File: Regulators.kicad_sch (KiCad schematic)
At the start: 26 parts, among them J5 24V Logic, J6 24V Peripheral, U2 TPS5430DDAR, U3 TPS5430DDAR

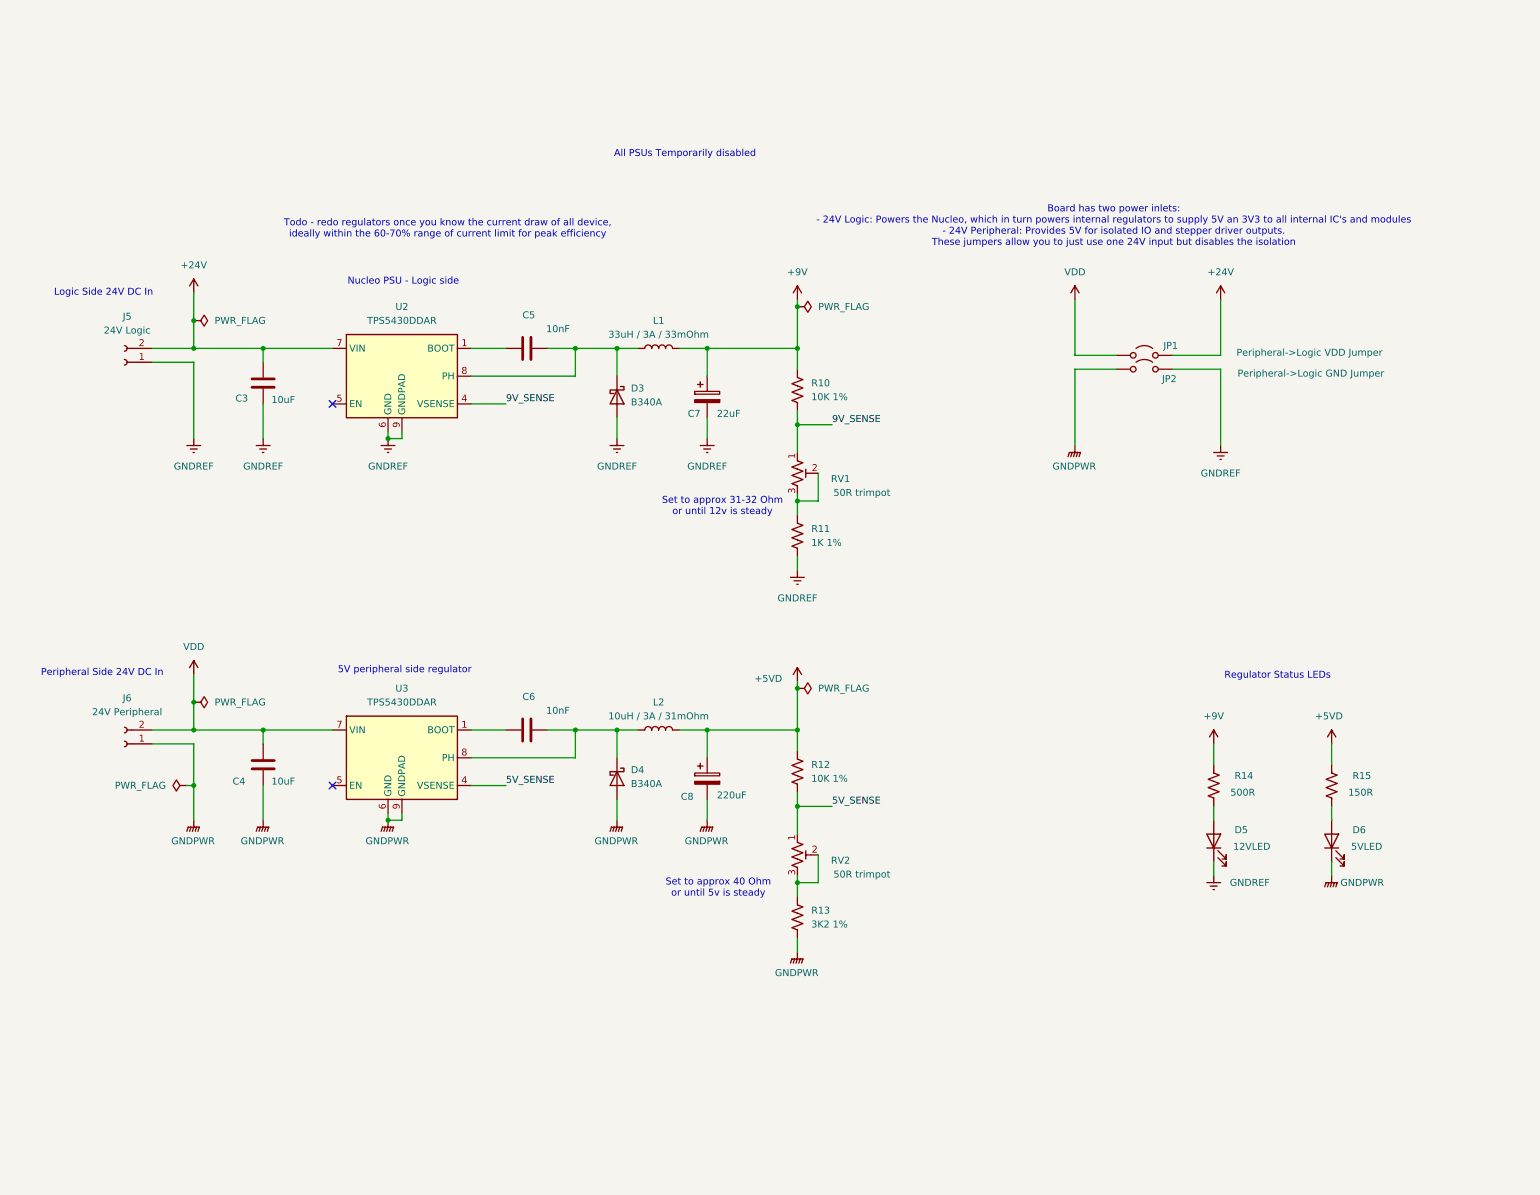
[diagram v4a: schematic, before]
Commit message: BOM consolidation for various resistors. Moved BOM into symbol libraries and updated supplimentary BOM. Switched IO optical isolation circuitry to a more cost effective part.
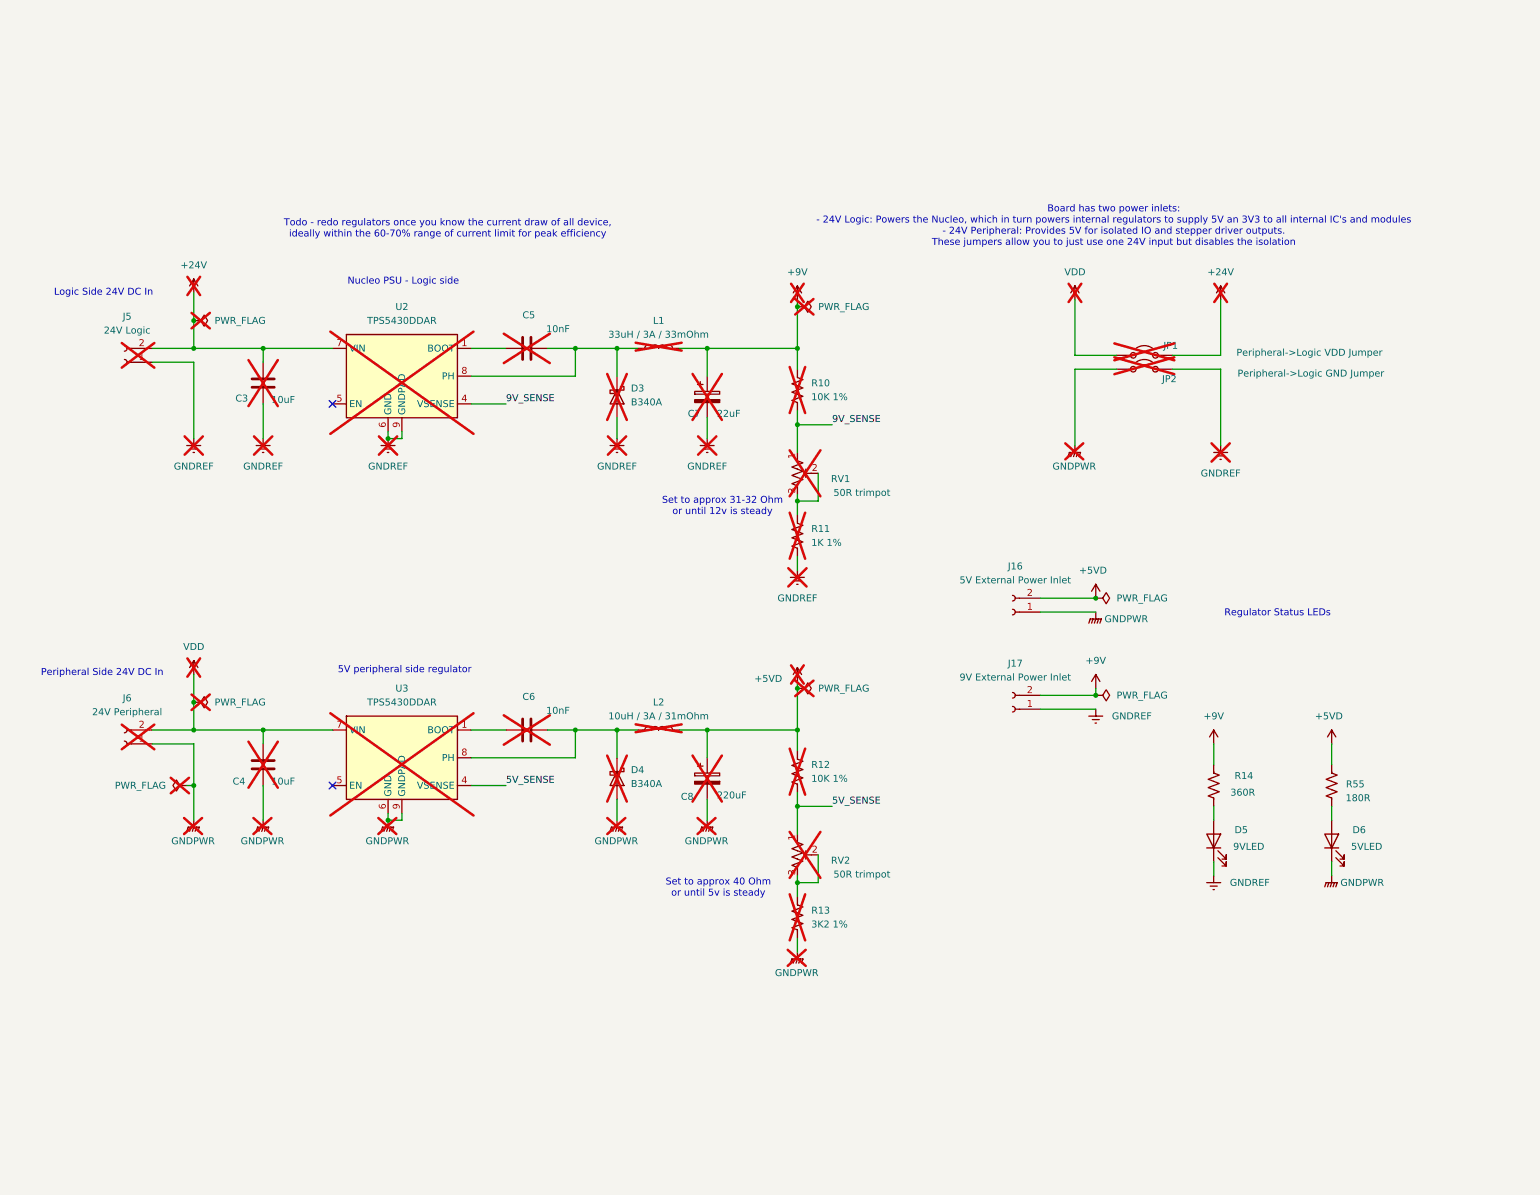
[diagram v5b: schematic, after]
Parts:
- removed R15: 150R, Resistor_SMD:R_1206_3216Metric_Pad1.30x1.75mm_HandSolder, symbol Device:R_US
- added J16: 5V External Power Inlet, EBWA_02_A:ADAMTECH_EBWA-02-A, symbol Connector:Conn_01x02_Socket
- added J17: 9V External Power Inlet, EBWA_02_A:ADAMTECH_EBWA-02-A, symbol Connector:Conn_01x02_Socket
- added R55: 180R, Resistor_SMD:R_1206_3216Metric_Pad1.30x1.75mm_HandSolder, symbol Device:R_US
- C3, C4, C5, C6, C7, C8, D3, D4, J5, J6, L1, L2, R10, R11, R12, R13: now not fitted
- D5: value 12VLED -> 9VLED
- JP1, JP2: Digikey Part Number (none) -> N/A; Digikey URL (none) -> N/A; now not fitted
- R14: value 500R -> 360R; Digikey Part Number (none) -> RMCF1206JT360RCT-ND; Digikey URL (none) -> https://www.digikey.com.au/en/products/detail/stackpole-ele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
- RV1, RV2: JLCPCB Part #（optional） C56340 -> (none); now not fitted
- U2, U3: JLCPCB Part #（optional） C9864 -> (none); now not fitted
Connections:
- net +5VD: now also J16.2 (Pin_2), R55.1
- net +9V: now also J17.2 (Pin_2)
- net GNDPWR: now also J16.1 (Pin_1)
- net GNDREF: now also J17.1 (Pin_1)
- net at D6.2 (A): now also R55.2
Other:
- note removed: "All PSUs Temporarily disabled"

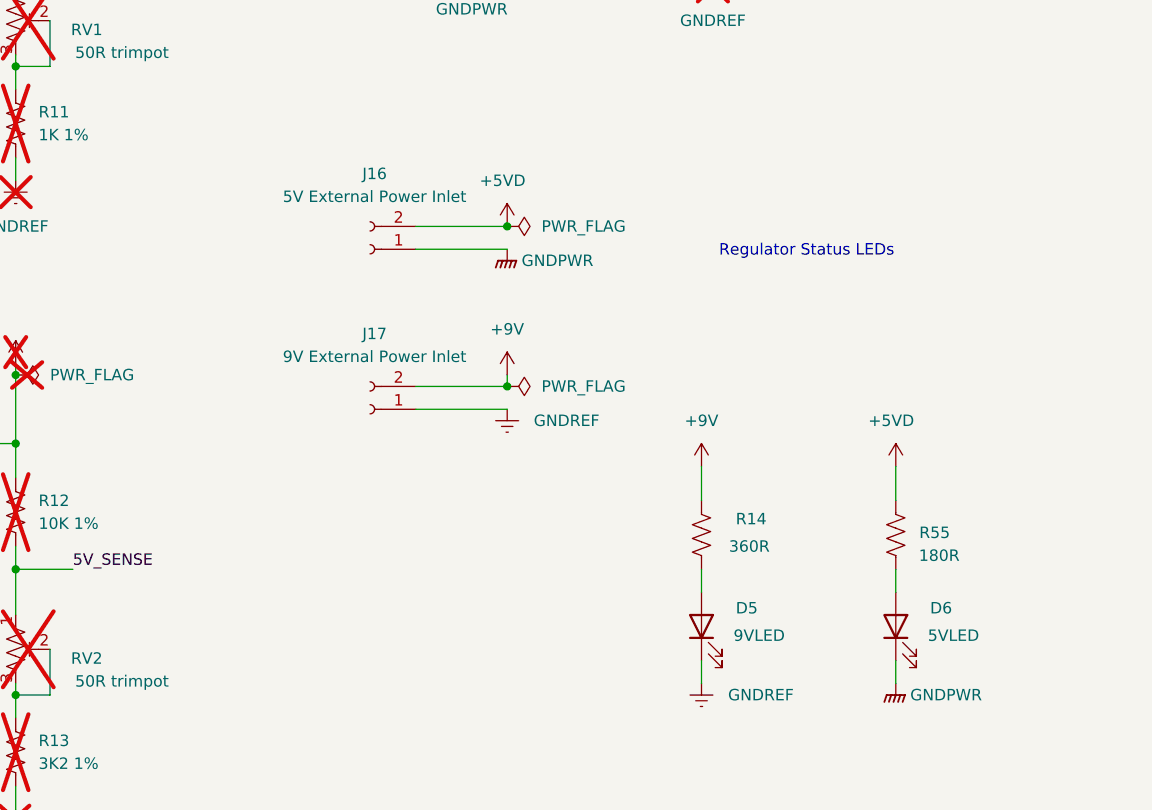
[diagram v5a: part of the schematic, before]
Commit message: more BOM consolidation. Switched out IO for vertical toolless wire to board terminals and added footprints. Put new isolated ground plane on board.
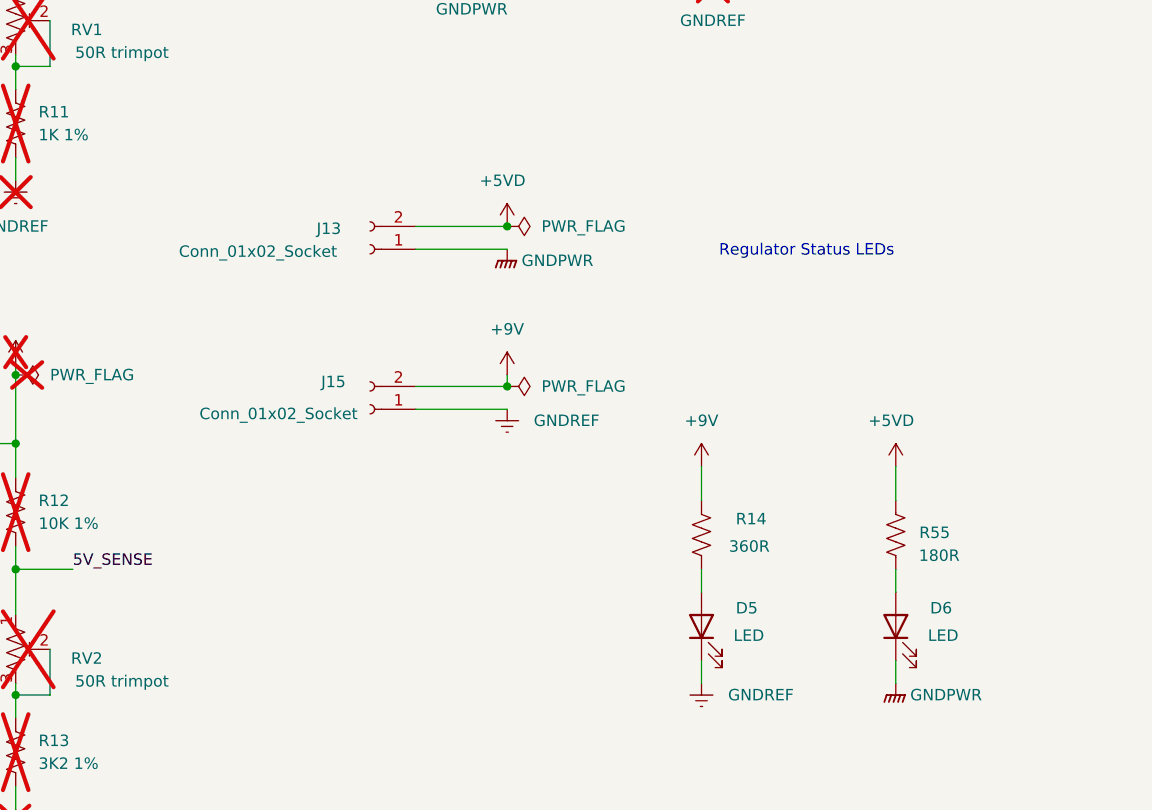
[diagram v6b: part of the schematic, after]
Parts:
- removed J16: 5V External Power Inlet, EBWA_02_A:ADAMTECH_EBWA-02-A, symbol Connector:Conn_01x02_Socket
- removed J17: 9V External Power Inlet, EBWA_02_A:ADAMTECH_EBWA-02-A, symbol Connector:Conn_01x02_Socket
- added J13, J15: Conn_01x02_Socket, Amphenol QT:QT02ADP83V0000G, symbol Connector:Conn_01x02_Socket
- D5: value 9VLED -> LED
- D6: value 5VLED -> LED
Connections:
- net +5VD: now also J13.2 (Pin_2)
- net +9V: now also J15.2 (Pin_2)
- net GNDPWR: now also J13.1 (Pin_1)
- net GNDREF: now also J15.1 (Pin_1)
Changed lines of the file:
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@@
-	)
-	(symbol
-		(lib_id "Connector:Conn_01x02_Socket")
-		(at 201.93 99.06 180)
-		(unit 1)
-		(exclude_from_sim no)
-		(in_bom yes)
-		(on_board yes)
-		(dnp no)
-		(property "Reference" "J16"
-			(at 202.438 90.678 0)
-			(effects
-				(font
-					(size 1.27 1.27)
-				)
-			)
-		)
-		(property "Value" "5V External Power Inlet"
-			(at 202.438 93.218 0)
-			(effects
-				(font
-					(size 1.27 1.27)
-				)
-			)
-		)
-		(property "Footprint" "EBWA_02_A:ADAMTECH_EBWA-02-A"
-			(at 201.93 99.06 0)
-			(effects
-				(font
-					(size 1.27 1.27)
-				)
-				(hide yes)
-			)
-		)
-		(property "Datasheet" "~"
-			(at 201.93 99.06 0)
-			(effects
-				(font
-					(size 1.27 1.27)
-				)
-				(hide yes)
-			)
-		)
-		(property "Description" "Generic connector, single row, 01x02, script generated"
-			(at 201.93 99.06 0)
-			(effects
-				(font
-					(size 1.27 1.27)
-				)
-				(hide yes)
-			)
-		)
-		(property "Digikey Part Number" "2057-EBWA-02-A-ND"
-			(at 201.93 99.06 0)
-			(effects
-				(font
-					(size 1.27 1.27)
-				)
-				(hide yes)
-			)
-		)
-		(property "Digikey URL" "https://www.digikey.com.au/en/products/detail/adam-tech/EBWA-02-A/9830631"
-			(at 201.93 99.06 0)
-			(effects
-				(font
-					(size 1.27 1.27)
-				)
-				(hide yes)
-			)
-		)
-		(pin "1"
-		)
-		(pin "2"
-		)
-		(instances
-			(project "Remora Nucleo F446ZE Hat"
-				(path "/5473abc6-7b93-43cc-a401-f691c4d7d7cf/e0dc83df-f7d9-4488-bd0b-6c0af36f8703"
-					(reference "J16")
-					(unit 1)
-				)
-			)
-		)
 	)
 	(symbol
@@
 			)
 		)
-		(property "Value" "5VLED"
+		(property "Value" "LED"
 			(at 263.906 141.986 90)
 			(effects
@@
 			)
 		)
-		(property "Value" "9VLED"
+		(property "Value" "LED"
 			(at 242.316 141.986 90)
 			(effects
@@
 	)
 	(symbol
-		(lib_id "Connector:Conn_01x02_Socket")
-		(at 201.93 116.84 180)
-		(unit 1)
-		(exclude_from_sim no)
-		(in_bom yes)
-		(on_board yes)
-		(dnp no)
-		(property "Reference" "J17"
-			(at 202.438 108.458 0)
-			(effects
-				(font
-					(size 1.27 1.27)
-				)
-			)
-		)
-		(property "Value" "9V External Power Inlet"
-			(at 202.438 110.998 0)
-			(effects
-				(font
-					(size 1.27 1.27)
-				)
-			)
-		)
-		(property "Footprint" "EBWA_02_A:ADAMTECH_EBWA-02-A"
-			(at 201.93 116.84 0)
-			(effects
-				(font
-					(size 1.27 1.27)
-				)
-				(hide yes)
-			)
-		)
-		(property "Datasheet" "~"
-			(at 201.93 116.84 0)
-			(effects
-				(font
-					(size 1.27 1.27)
-				)
-				(hide yes)
-			)
-		)
-		(property "Description" "Generic connector, single row, 01x02, script generated"
-			(at 201.93 116.84 0)
-			(effects
-				(font
-					(size 1.27 1.27)
-				)
-				(hide yes)
-			)
-		)
-		(property "Digikey Part Number" "2057-EBWA-02-A-ND"
-			(at 201.93 116.84 0)
-			(effects
-				(font
-					(size 1.27 1.27)
-				)
-				(hide yes)
-			)
-		)
-		(property "Digikey URL" "https://www.digikey.com.au/en/products/detail/adam-tech/EBWA-02-A/9830631"
-			(at 201.93 116.84 0)
-			(effects
-				(font
-					(size 1.27 1.27)
-				)
-				(hide yes)
-			)
-		)
-		(pin "1"
-		)
-		(pin "2"
-		)
-		(instances
-			(project "Remora Nucleo F446ZE Hat"
-				(path "/5473abc6-7b93-43cc-a401-f691c4d7d7cf/e0dc83df-f7d9-4488-bd0b-6c0af36f8703"
-					(reference "J17")
-					(unit 1)
-				)
-			)
-		)
-	)
-	(symbol
 		(lib_id "power:PWR_FLAG")
 		(at 52.07 115.57 270)
@@
 	)
 	(symbol
+		(lib_id "Connector:Conn_01x02_Socket")
+		(at 201.93 116.84 180)
+		(unit 1)
+		(exclude_from_sim no)
+		(in_bom yes)
+		(on_board yes)
+		(dnp no)
+		(property "Reference" "J15"
+			(at 197.866 113.792 0)
+			(effects
+				(font
+					(size 1.27 1.27)
+				)
+			)
+		)
+		(property "Value" "Conn_01x02_Socket"
+			(at 191.77 117.348 0)
+			(effects
+				(font
+					(size 1.27 1.27)
+				)
+			)
+		)
+		(property "Footprint" "Amphenol QT:QT02ADP83V0000G"
+			(at 201.93 116.84 0)
+			(effects
+				(font
+					(size 1.27 1.27)
+				)
+				(hide yes)
+			)
+		)
+		(property "Datasheet" "~"
+			(at 201.93 116.84 0)
+			(effects
+				(font
+					(size 1.27 1.27)
+				)
+				(hide yes)
+			)
+		)
+		(property "Description" "Generic connector, single row, 01x02, script generated"
+			(at 201.93 116.84 0)
+			(effects
+				(font
+					(size 1.27 1.27)
+				)
+				(hide yes)
+			)
+		)
+		(property "Digikey Part Number" "1818-QT04ADP83V0000G-ND"
+			(at 202.565 109.22 0)
+			(effects
+				(font
+					(size 1.27 1.27)
+				)
+				(hide yes)
+			)
+		)
+		(property "Digikey URL" "https://www.digikey.com.au/en/products/detail/amphenol-anytek/QT04ADP83V0000G/25618782"
+			(at 202.565 111.76 0)
+			(effects
+				(font
+					(size 1.27 1.27)
+				)
+				(hide yes)
+			)
+		)
+		(pin "1"
+		)
+		(pin "2"
+		)
+		(instances
+			(project "Remora Nucleo F446ZE Hat"
+				(path "/5473abc6-7b93-43cc-a401-f691c4d7d7cf/e0dc83df-f7d9-4488-bd0b-6c0af36f8703"
+					(reference "J15")
+					(unit 1)
+				)
+			)
+		)
+	)
+	(symbol
 		(lib_id "Device:R_US")
 		(at 162.56 154.94 0)
@@
 					(unit 1)
 				)
+			)
+		)
+	)
+	(symbol
+		(lib_id "Connector:Conn_01x02_Socket")
+		(at 201.93 99.06 180)
+		(unit 1)
+		(exclude_from_sim no)
+		(in_bom yes)
+		(on_board yes)
+		(dnp no)
+		(property "Reference" "J13"
+			(at 197.358 96.774 0)
+			(effects
+				(font
+					(size 1.27 1.27)
+				)
+			)
+		)
+		(property "Value" "Conn_01x02_Socket"
+			(at 189.484 99.314 0)
+			(effects
+				(font
+					(size 1.27 1.27)
+				)
+			)
+		)
+		(property "Footprint" "Amphenol QT:QT02ADP83V0000G"
+			(at 201.93 99.06 0)
+			(effects
+				(font
+					(size 1.27 1.27)
+				)
+				(hide yes)
+			)
+		)
+		(property "Datasheet" "~"
+			(at 201.93 99.06 0)
+			(effects
+				(font
+					(size 1.27 1.27)
+				)
+				(hide yes)
+			)
+		)
+		(property "Description" "Generic connector, single row, 01x02, script generated"
+			(at 201.93 99.06 0)
+			(effects
+				(font
+					(size 1.27 1.27)
+				)
+				(hide yes)
+			)
+		)
+		(property "Digikey Part Number" "1818-QT04ADP83V0000G-ND"
+			(at 202.565 91.44 0)
+			(effects
+				(font
+					(size 1.27 1.27)
+				)
+				(hide yes)
+			)
+		)
+		(property "Digikey URL" "https://www.digikey.com.au/en/products/detail/amphenol-anytek/QT04ADP83V0000G/25618782"
+			(at 202.565 93.98 0)
+			(effects
+				(font
+					(size 1.27 1.27)
+				)
+				(hide yes)
+			)
+		)
+		(pin "1"
+		)
+		(pin "2"
+		)
+		(instances
+			(project "Remora Nucleo F446ZE Hat"
+				(path "/5473abc6-7b93-43cc-a401-f691c4d7d7cf/e0dc83df-f7d9-4488-bd0b-6c0af36f8703"
+					(reference "J13")
+					(unit 1)
+				)

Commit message: New PSU schematics
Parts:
- removed C5, C6: 10nF, Capacitor_SMD:C_1206_3216Metric_Pad1.33x1.80mm_HandSolder, symbol Device:C
- removed J13, J15: Conn_01x02_Socket, Amphenol QT:QT02ADP83V0000G, symbol Connector:Conn_01x02_Socket
- removed R10, R12: 10K 1%, Resistor_SMD:R_1206_3216Metric_Pad1.30x1.75mm_HandSolder, symbol Device:R_US
- removed R11: 1K 1%, Resistor_SMD:R_1206_3216Metric_Pad1.30x1.75mm_HandSolder, symbol Device:R_US
- removed R13: 3K2 1%, Resistor_SMD:R_1206_3216Metric_Pad1.30x1.75mm_HandSolder, symbol Device:R_US
- removed RV1, RV2: 50R trimpot, Potentiometer_SMD:Potentiometer_Bourns_3224W_Vertical, symbol Device:R_Potentiometer_Trim_US
- removed U2, U3: TPS5430DDAR, Package_SO:TI_SO-PowerPAD-8_ThermalVias, symbol Regulator_Switching:TPS5430DDA
- added C10, C9: 470uF, symbol Device:C_Polarized
- added U?: XL1509-12, Package_SO:SOIC-8_3.9x4.9mm_P1.27mm, symbol Regulator_Switching:XL1509-12
- added U?: XL1509-5.0, Package_SO:SOIC-8_3.9x4.9mm_P1.27mm, symbol Regulator_Switching:XL1509-5.0
- C3, C4: value 10uF -> 1uF; now fitted
- C7: value 22uF -> 180uF; now fitted
- C8: value 220uF -> 180uF; now fitted
- D3, D4: value B340A -> 1N5821; now fitted
- J5, J6, JP1, JP2: now fitted
- L1: value 33uH / 3A / 33mOhm -> 68uH / 1A; now fitted
- L2: value 10uH / 3A / 31mOhm -> 68uH / 1A; now fitted
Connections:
- net +24V: now also C9.1, U?.1 (VIN)
- net +5VD: now also U?.3 (FB)
- net GNDPWR: now also C10.2, U?.4 (~{EN}), U?.5 (GND), U?.6 (GND), U?.7 (GND), U?.8 (GND)
- net GNDREF: now also C9.2, U?.4 (~{EN}), U?.5 (GND), U?.6 (GND), U?.7 (GND), U?.8 (GND)
- net VDD: now also C10.1, U?.1 (VIN)
- net at D4.1 (K), L2.1: now also U?.2 (OUT)
- net at D3.1 (K), L1.1: now also U?.2 (OUT)
- net +9V renamed +12V
- net +12V: now also U?.3 (FB)
- no-connect marks 2 -> 0
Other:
- note removed: "Set to approx 31-32 Ohm or until 12v is steady"
- note removed: "Set to approx 40 Ohm or until 5v is steady"
- note removed: "Todo - redo regulators once you know the current draw of all device, ideally within the 60-70% range of current limit for peak efficiency"
- moved on the sheet: D5, D6, R14, R55
